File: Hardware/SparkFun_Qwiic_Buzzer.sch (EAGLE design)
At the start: 48 parts, among them J2 QWIIC_RA, J3 QWIIC_RA, Q3 200mA/40V, U4 ATTINY84-ARDUINO

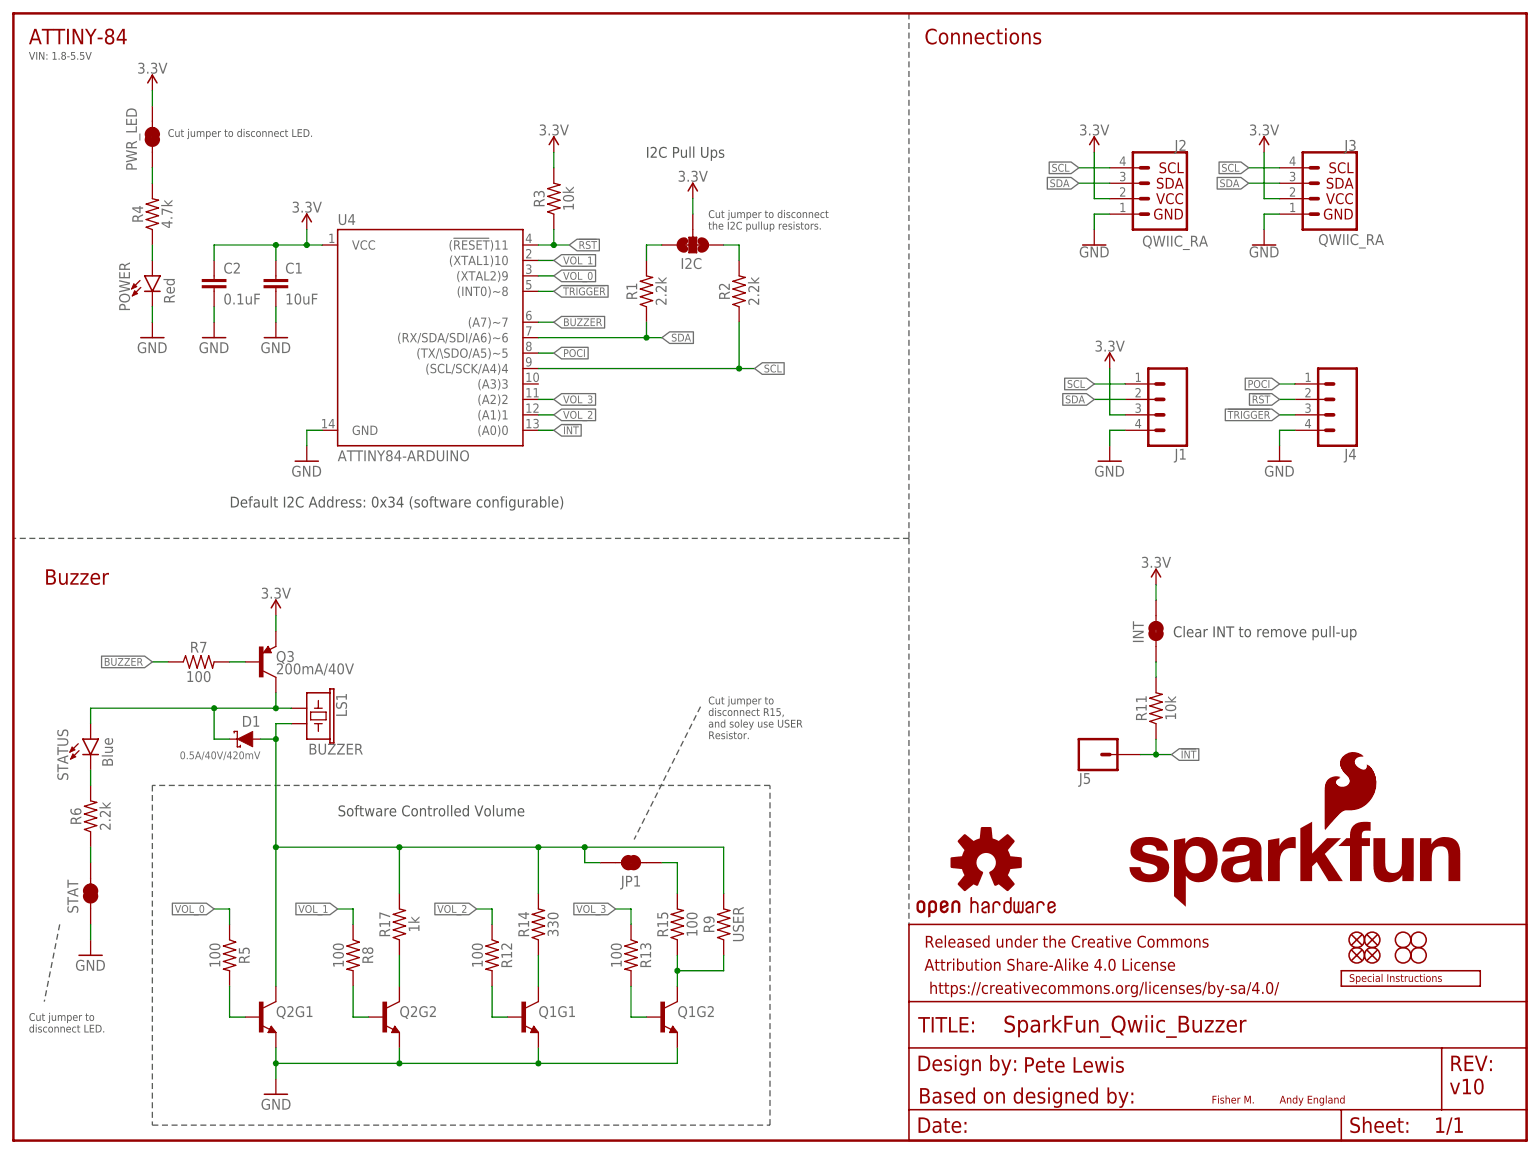
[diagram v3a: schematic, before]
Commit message: Corrected GND header silk label
-rotated GND header silk label to match others
-updated VCC note in sch to show typically 3.3V via QWIIC.
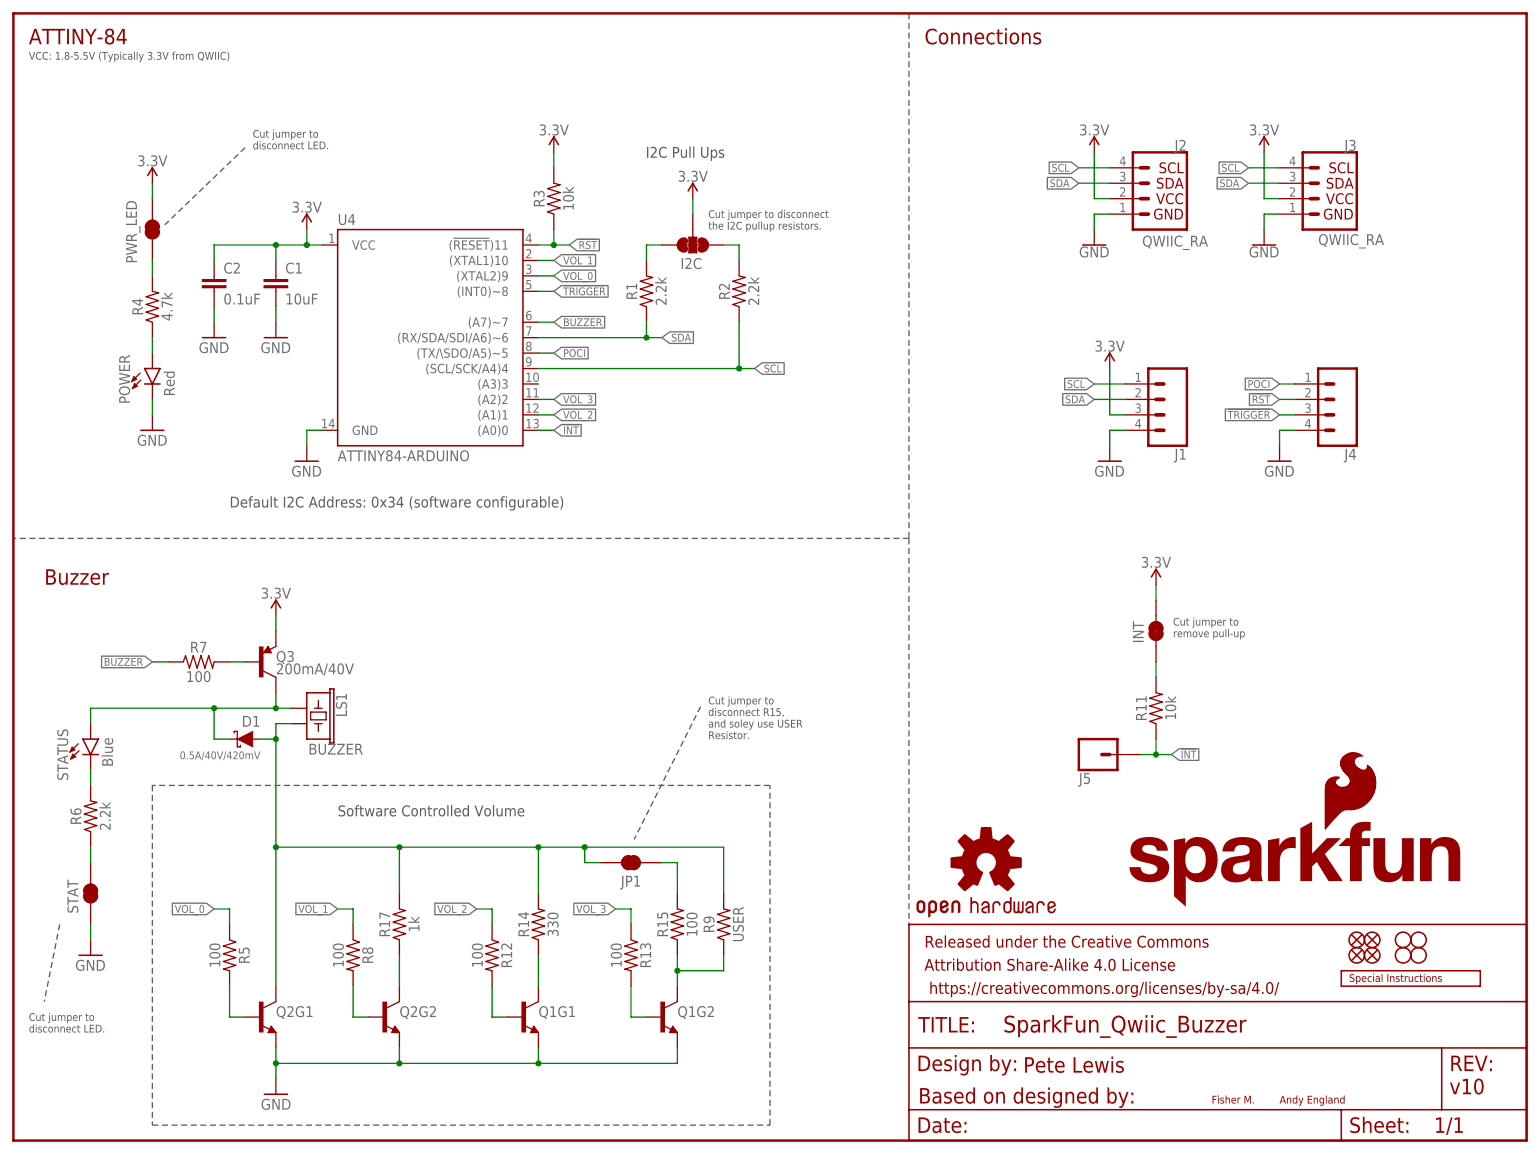
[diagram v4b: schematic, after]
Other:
- note added: "Cut jumper to remove pull-up"
- note added: "VCC: 1.8-5.5V (Typically 3.3V from QWIIC)"
- note removed: "Clear INT to remove pull-up"
- note removed: "VIN: 1.8-5.5V"
- moved on the sheet: POWER, PWR_LED, R4
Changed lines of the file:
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@@
 the I2C pullup resistors.</text>
 <text x="104.013" y="161.671" size="1.778" layer="97" font="vector">I2C Pull Ups</text>
-<text x="190.754" y="82.804" size="1.778" layer="97" font="vector">Clear INT to remove pull-up</text>
+<text x="190.754" y="82.804" size="1.27" layer="97" font="vector">Cut jumper to
+remove pull-up</text>
 <text x="197.104" y="6.096" size="1.27" layer="94" font="vector">Fisher M.</text>
 <text x="208.28" y="6.096" size="1.27" layer="94" font="vector">Andy England</text>
@@
 <wire x1="147.32" y1="99.06" x2="0" y2="99.06" width="0.1524" layer="97" style="longdash"/>
 <text x="5.08" y="91.44" size="2.54" layer="94" font="vector">Buzzer</text>
-<text x="2.54" y="177.8" size="1.27" layer="97" font="vector">VIN: 1.8-5.5V</text>
+<text x="2.54" y="177.8" size="1.27" layer="97" font="vector">VCC: 1.8-5.5V (Typically 3.3V from QWIIC)</text>
 <text x="148.844" y="6.096" size="2.54" layer="94" font="vector">Based on designed by:</text>
 <text x="166.116" y="11.176" size="2.54" layer="94" font="vector">Pete Lewis</text>
@@
 <wire x1="22.86" y1="2.54" x2="124.46" y2="2.54" width="0.1524" layer="97" style="shortdash"/>
 <wire x1="124.46" y1="2.54" x2="124.46" y2="58.42" width="0.1524" layer="97" style="shortdash"/>
-<text x="25.4" y="165.1" size="1.27" layer="97" font="vector">Cut jumper to disconnect LED.</text>
+<text x="39.37" y="163.068" size="1.27" layer="97" font="vector">Cut jumper to
+disconnect LED.</text>
 <text x="2.54" y="17.78" size="1.27" layer="97" font="vector">Cut jumper to
 disconnect LED.</text>
@@
 Resistor.</text>
 <wire x1="113.03" y1="71.374" x2="102.108" y2="49.53" width="0.1524" layer="97" style="shortdash"/>
+<wire x1="38.1" y1="163.322" x2="24.892" y2="150.622" width="0.1524" layer="97" style="shortdash"/>
 </plain>
 <instances>
@@
 <attribute name="NAME" x="109.728" y="143.383" size="1.778" layer="95" font="vector"/>
 </instance>
-<instance part="R4" gate="G$1" x="22.86" y="152.4" smashed="yes" rot="R90">
-<attribute name="NAME" x="21.336" y="152.4" size="1.778" layer="95" font="vector" rot="R90" align="bottom-center"/>
-<attribute name="VALUE" x="24.384" y="152.4" size="1.778" layer="96" font="vector" rot="R90" align="top-center"/>
-</instance>
-<instance part="POWER" gate="G$1" x="22.86" y="142.24" smashed="yes">
-<attribute name="NAME" x="19.177" y="136.398" size="1.778" layer="95" font="vector" rot="R90"/>
-<attribute name="VALUE" x="24.765" y="137.668" size="1.778" layer="96" font="vector" rot="R90" align="top-left"/>
-</instance>
-<instance part="GND10" gate="1" x="22.86" y="132.08" smashed="yes">
-<attribute name="VALUE" x="20.32" y="129.54" size="1.778" layer="96" font="vector"/>
+<instance part="R4" gate="G$1" x="22.86" y="137.16" smashed="yes" rot="R90">
+<attribute name="NAME" x="21.336" y="137.16" size="1.778" layer="95" font="vector" rot="R90" align="bottom-center"/>
+<attribute name="VALUE" x="24.384" y="137.16" size="1.778" layer="96" font="vector" rot="R90" align="top-center"/>
+</instance>
+<instance part="POWER" gate="G$1" x="22.86" y="127" smashed="yes">
+<attribute name="NAME" x="19.177" y="121.158" size="1.778" layer="95" font="vector" rot="R90"/>
+<attribute name="VALUE" x="24.765" y="122.428" size="1.778" layer="96" font="vector" rot="R90" align="top-left"/>
+</instance>
+<instance part="GND10" gate="1" x="22.86" y="116.84" smashed="yes">
+<attribute name="VALUE" x="20.32" y="114.3" size="1.778" layer="96" font="vector"/>
 </instance>
 <instance part="J5" gate="J1" x="177.8" y="63.5" smashed="yes" rot="MR180">
@@
 <attribute name="VALUE" x="34.036" y="30.48" size="1.778" layer="96" font="vector" rot="R270" align="top-center"/>
 </instance>
-<instance part="PWR_LED" gate="G$1" x="22.86" y="165.1" smashed="yes" rot="R90">
-<attribute name="NAME" x="20.32" y="159.512" size="1.778" layer="95" font="vector" rot="R90"/>
-</instance>
-<instance part="SUPPLY3" gate="G$1" x="22.86" y="172.72" smashed="yes">
-<attribute name="VALUE" x="22.86" y="175.514" size="1.778" layer="96" font="vector" align="bottom-center"/>
+<instance part="PWR_LED" gate="G$1" x="22.86" y="149.86" smashed="yes" rot="R90">
+<attribute name="NAME" x="20.32" y="144.272" size="1.778" layer="95" font="vector" rot="R90"/>
+</instance>
+<instance part="SUPPLY3" gate="G$1" x="22.86" y="157.48" smashed="yes">
+<attribute name="VALUE" x="22.86" y="160.274" size="1.778" layer="96" font="vector" align="bottom-center"/>
 </instance>
 <instance part="GND9" gate="1" x="43.18" y="7.62" smashed="yes" rot="MR0">
@@
 <pinref part="POWER" gate="G$1" pin="C"/>
 <pinref part="GND10" gate="1" pin="GND"/>
-<wire x1="22.86" y1="134.62" x2="22.86" y2="137.16" width="0.1524" layer="91"/>
+<wire x1="22.86" y1="119.38" x2="22.86" y2="121.92" width="0.1524" layer="91"/>
 </segment>
 <segment>
@@
 </segment>
 <segment>
-<wire x1="22.86" y1="170.18" x2="22.86" y2="172.72" width="0.1524" layer="91"/>
+<wire x1="22.86" y1="154.94" x2="22.86" y2="157.48" width="0.1524" layer="91"/>
 <pinref part="SUPPLY3" gate="G$1" pin="3.3V"/>
 <pinref part="PWR_LED" gate="G$1" pin="2"/>
@@
 <pinref part="R4" gate="G$1" pin="1"/>
 <pinref part="POWER" gate="G$1" pin="A"/>
-<wire x1="22.86" y1="144.78" x2="22.86" y2="147.32" width="0.1524" layer="91"/>
+<wire x1="22.86" y1="129.54" x2="22.86" y2="132.08" width="0.1524" layer="91"/>
 </segment>
 </net>
@@
 <pinref part="R4" gate="G$1" pin="2"/>
 <pinref part="PWR_LED" gate="G$1" pin="1"/>
-<wire x1="22.86" y1="160.02" x2="22.86" y2="157.48" width="0.1524" layer="91"/>
-</segment>
-</net>
+<wire x1="22.86" y1="144.78" x2="22.86" y2="142.24" width="0.1524" layer="91"/>
+</segment>
+</net>

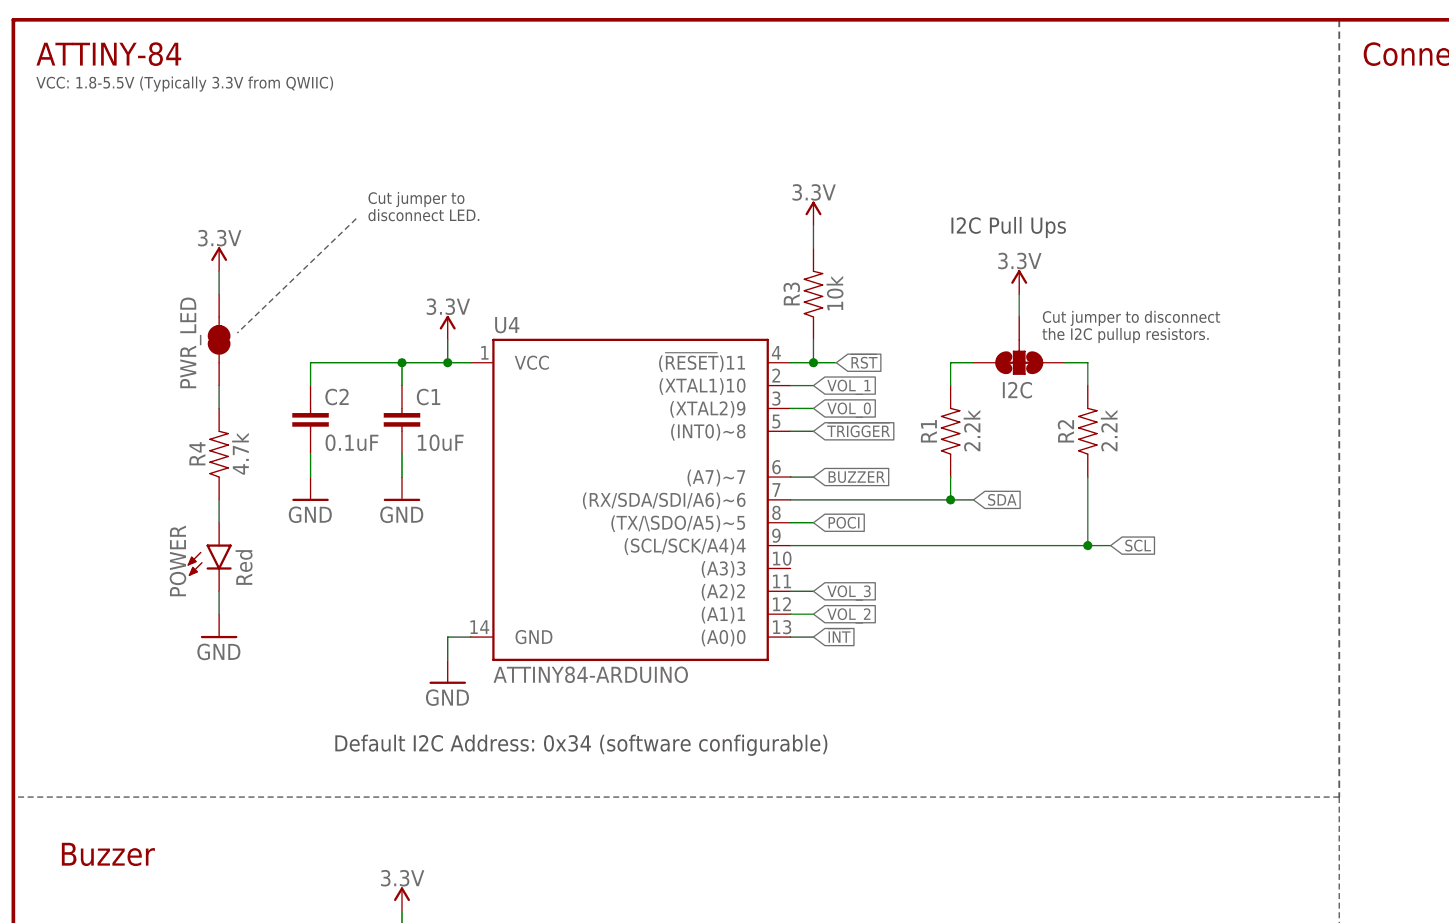
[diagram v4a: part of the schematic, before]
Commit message: Added note about SPI - only for programming
-This product will not accept commands via SPI. These connections are only broken out for firmware programming.
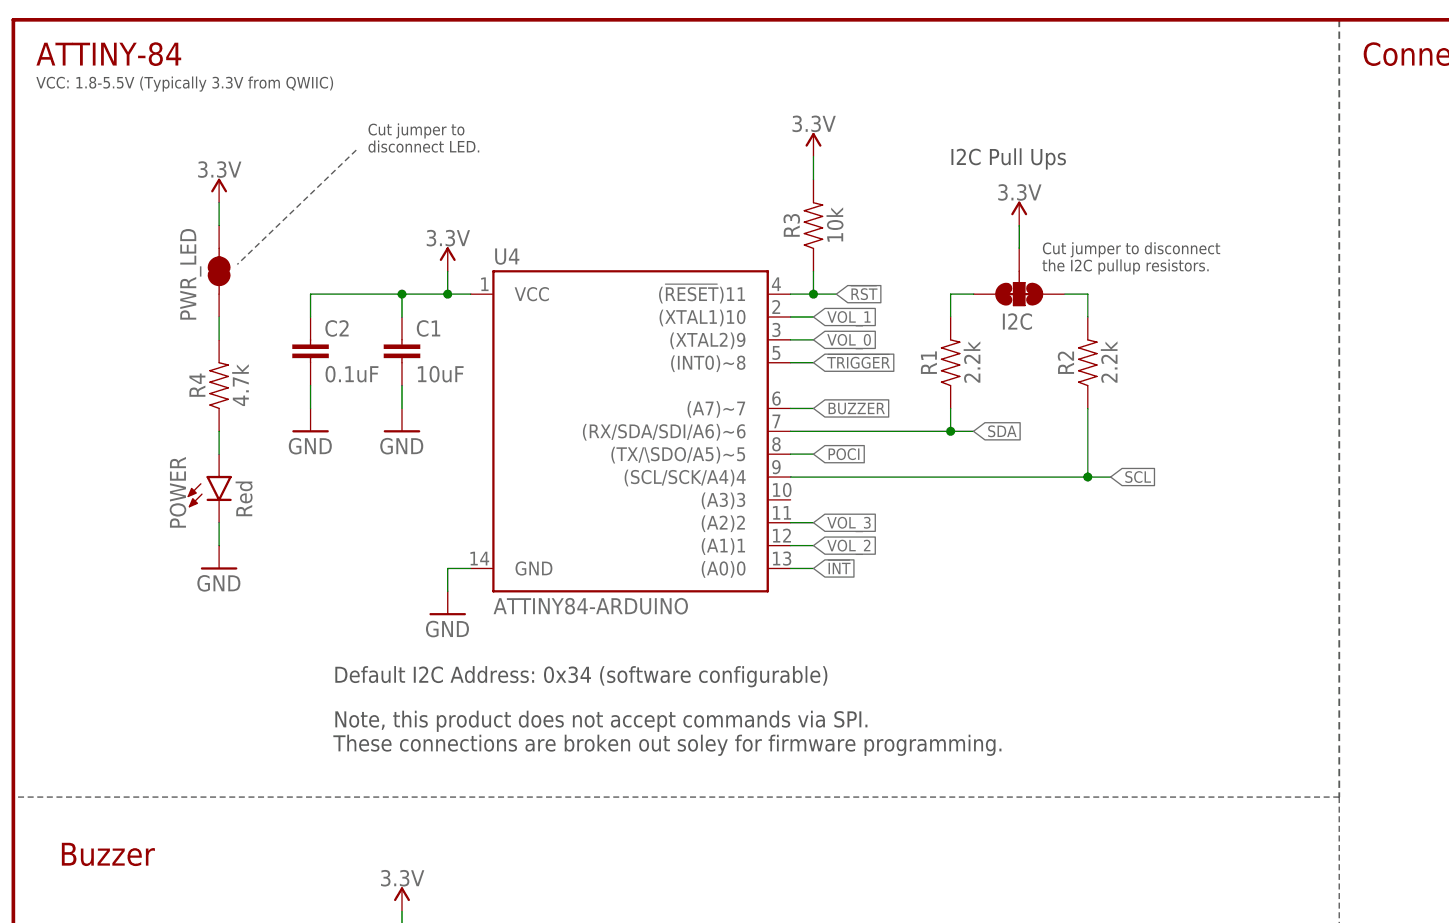
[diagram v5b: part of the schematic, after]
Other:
- note added: "Note, this product does not accept commands via SPI. These connections are broken out soley for firmware programming."
- moved on the sheet: C1, C2, I2C, POWER, PWR_LED, R1, R2, R3, R4, U4
